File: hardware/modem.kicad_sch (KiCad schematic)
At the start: 30 parts, among them J11 Conn_01x02, Q3 PMOS, Q4 Q_NPN_BEC, U6 SN74AVC4T245PW, U7 SARA-R500S-61B

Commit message: HW: Update BOM
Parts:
- J11: value Conn_01x02 -> PRPC001DAAN-RC
- Q3: value PMOS -> FDN338P
- Q4: value Q_NPN_BEC -> MMBT3904-TP
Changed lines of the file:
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@@
 			)
 		)
-		(property "Value" "PMOS"
+		(property "Value" "FDN338P"
 			(at 30.48 84.836 90)
 			(effects
@@
 			)
 		)
-		(property "Value" "Conn_01x02"
+		(property "Value" "PRPC001DAAN-RC"
 			(at 49.53 163.83 0)
 			(effects
@@
 			)
 		)
-		(property "Value" "Q_NPN_BEC"
+		(property "Value" "MMBT3904-TP"
 			(at 64.77 165.0999 0)
 			(effects

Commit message: HW: Fix BOM
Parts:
- TP5: now left out of the parts list
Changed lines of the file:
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@@
 		(unit 1)
 		(exclude_from_sim no)
-		(in_bom yes)
+		(in_bom no)
 		(on_board yes)
 		(dnp no)

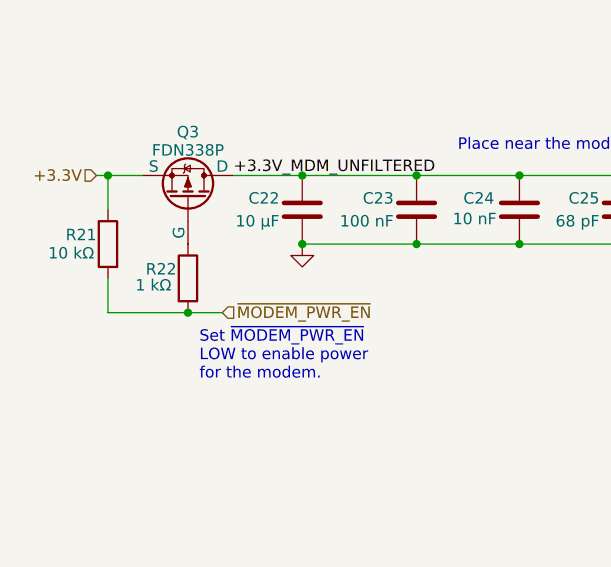
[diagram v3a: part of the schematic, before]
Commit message: HW: BOM consolidate
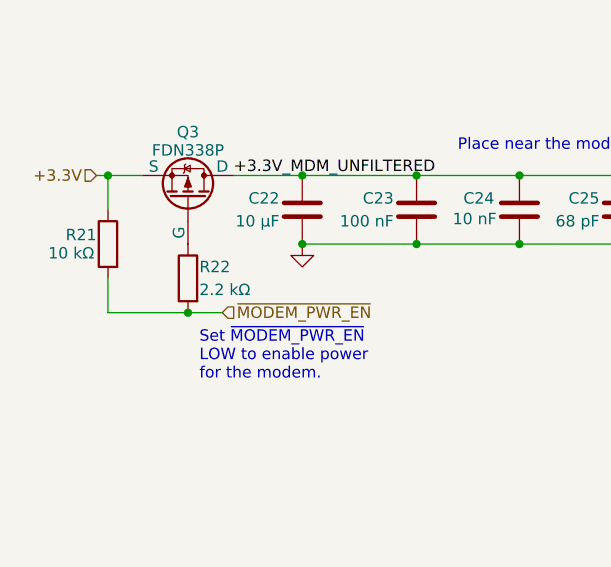
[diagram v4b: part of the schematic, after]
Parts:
- R22: value 1 kΩ -> 2.2 kΩ; Digi-Key Part Number 311-1.00KLRCT-ND -> 311-2.20KLRCT-ND; Manufacturer Part Number RC0402FR-071KL -> RC0402FR-072K2L
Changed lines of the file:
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@@
 	)
 	(junction
-		(at 30.48 102.87)
-		(diameter 0)
-		(color 0 0 0 0)
-	)
-	(junction
 		(at 170.18 101.6)
 		(diameter 0)
@@
 	)
 	(junction
+		(at 30.48 102.87)
+		(diameter 0)
+		(color 0 0 0 0)
+	)
+	(junction
 		(at 83.82 163.83)
 		(diameter 0)
@@
 	(wire
 		(pts
-			(xy 34.29 102.87) (xy 30.48 102.87)
+			(xy 55.88 87.63) (xy 67.31 87.63)
 		)
 		(stroke
@@
 	(wire
 		(pts
-			(xy 55.88 87.63) (xy 67.31 87.63)
+			(xy 154.94 83.82) (xy 157.48 83.82)
 		)
 		(stroke
@@
 	(wire
 		(pts
-			(xy 154.94 83.82) (xy 157.48 83.82)
+			(xy 270.51 109.22) (xy 274.32 109.22)
 		)
 		(stroke
@@
 	(wire
 		(pts
-			(xy 270.51 109.22) (xy 274.32 109.22)
+			(xy 66.04 156.21) (xy 67.31 156.21)
 		)
 		(stroke
@@
 	(wire
 		(pts
-			(xy 66.04 156.21) (xy 67.31 156.21)
+			(xy 30.48 102.87) (xy 34.29 102.87)
 		)
 		(stroke
@@
 	)
 	(symbol
-		(lib_id "Device:R")
-		(at 30.48 99.06 0)
+		(lib_id "power:GND")
+		(at 255.27 162.56 0)
+		(mirror y)
 		(unit 1)
 		(exclude_from_sim no)
@@
 		(on_board yes)
 		(dnp no)
-		(property "Reference" "R22"
-			(at 29.21 98.044 0)
-			(effects
-				(font
-					(size 1.27 1.27)
-				)
-				(justify right)
-			)
-		)
-		(property "Value" "1 kΩ"
-			(at 24.638 99.822 0)
-			(effects
-				(font
-					(size 1.27 1.27)
-				)
-				(justify left)
-			)
-		)
-		(property "Footprint" "perfect_footprints:0402_1005_perfect"
-			(at 28.702 99.06 90)
-			(effects
-				(font
-					(size 1.27 1.27)
-				)
-				(hide yes)
-			)
-		)
-		(property "Datasheet" "~"
-			(at 30.48 99.06 0)
+		(fields_autoplaced yes)
+		(property "Reference" "#PWR026"
+			(at 255.27 168.91 0)
 			(effects
 				(font
@@
 			)
 		)
-		(property "Description" ""
-			(at 30.48 99.06 0)
+		(property "Value" "GND"
+			(at 255.27 167.64 0)
 			(effects
 				(font
@@
 			)
 		)
-		(property "Manufacturer" "YAGEO"
-			(at 30.48 99.06 0)
+		(property "Footprint" ""
+			(at 255.27 162.56 0)
 			(effects
 				(font
@@
 			)
 		)
-		(property "Manufacturer Part Number" "RC0402FR-071KL"
-			(at 30.48 99.06 0)
+		(property "Datasheet" ""
+			(at 255.27 162.56 0)
 			(effects
 				(font
@@
 			)
 		)
-		(property "Digi-Key Part Number" "311-1.00KLRCT-ND"
-			(at 30.48 99.06 0)
+		(property "Description" "Power symbol creates a global label with name \"GND\" , ground"
+			(at 255.27 162.56 0)
 			(effects
 				(font
@@
 		(pin "1"
 		)
-		(pin "2"
-		)
 		(instances
 			(project "iida_devkit"
 				(path "/b12a6e25-97fb-4aba-bc96-af8db389bb9a/3723475b-e956-4027-ac40-e47346743900"
-					(reference "R22")
+					(reference "#PWR026")
 					(unit 1)
 				)
@@
 	)
 	(symbol
-		(lib_id "power:GND")
-		(at 255.27 162.56 0)
+		(lib_id "Device:R")
+		(at 30.48 99.06 0)
 		(mirror y)
 		(unit 1)
@@
 		(on_board yes)
 		(dnp no)
-		(fields_autoplaced yes)
-		(property "Reference" "#PWR026"
-			(at 255.27 168.91 0)
+		(property "Reference" "R22"
+			(at 31.75 97.79 0)
+			(effects
+				(font
+					(size 1.27 1.27)
+				)
+				(justify right)
+			)
+		)
+		(property "Value" "2.2 kΩ"
+			(at 31.75 100.33 0)
+			(effects
+				(font
+					(size 1.27 1.27)
+				)
+				(justify right)
+			)
+		)
+		(property "Footprint" "perfect_footprints:0402_1005_perfect"
+			(at 32.258 99.06 90)
 			(effects
 				(font
@@
 			)
 		)
-		(property "Value" "GND"
-			(at 255.27 167.64 0)
+		(property "Datasheet" "~"
+			(at 30.48 99.06 0)
 			(effects
 				(font
@@
 			)
 		)
-		(property "Footprint" ""
-			(at 255.27 162.56 0)
+		(property "Description" ""
+			(at 30.48 99.06 0)
 			(effects
 				(font
@@
 			)
 		)
-		(property "Datasheet" ""
-			(at 255.27 162.56 0)
+		(property "Digi-Key Part Number" "311-2.20KLRCT-ND"
+			(at 30.48 99.06 0)
 			(effects
 				(font
@@
 			)
 		)
-		(property "Description" "Power symbol creates a global label with name \"GND\" , ground"
-			(at 255.27 162.56 0)
+		(property "Manufacturer" "YAGEO"
+			(at 30.48 99.06 0)
+			(effects
+				(font
+					(size 1.27 1.27)
+				)
+				(hide yes)
+			)
+		)
+		(property "Manufacturer Part Number" "RC0402FR-072K2L"
+			(at 30.48 99.06 0)
 			(effects
 				(font
@@
 			)
 		)
+		(pin "2"
+		)
 		(pin "1"
 		)
@@
 			(project "iida_devkit"
 				(path "/b12a6e25-97fb-4aba-bc96-af8db389bb9a/3723475b-e956-4027-ac40-e47346743900"
-					(reference "#PWR026")
+					(reference "R22")
 					(unit 1)
 				)

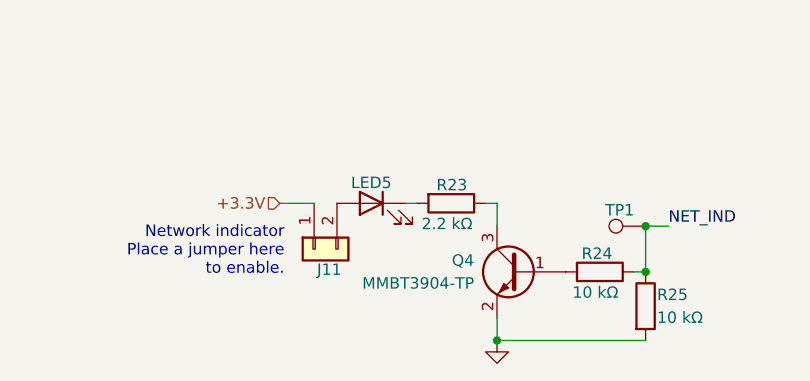
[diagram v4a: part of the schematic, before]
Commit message: HW: Replace chinese NPN BJT
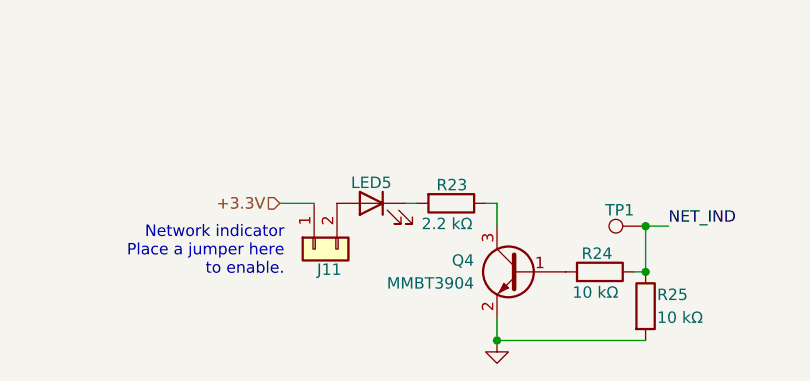
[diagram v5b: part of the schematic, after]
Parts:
- Q4: value MMBT3904-TP -> MMBT3904; Digi-Key Part Number MMBT3904TPMSCT-ND -> 4878-MMBT3904CT-ND; Manufacturer Micro Commercial Co -> Diotec Semiconductor; Manufacturer Part Number MMBT3904-TP -> MMBT3904
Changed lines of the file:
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@@
 			)
 		)
-		(property "Value" "MMBT3904-TP"
+		(property "Value" "MMBT3904"
 			(at 64.77 165.0999 0)
 			(effects
@@
 			)
 		)
-		(property "Digi-Key Part Number" "MMBT3904TPMSCT-ND"
+		(property "Digi-Key Part Number" "4878-MMBT3904CT-ND"
 			(at 69.85 163.83 0)
 			(effects
@@
 			)
 		)
-		(property "Manufacturer" "Micro Commercial Co"
+		(property "Manufacturer" "Diotec Semiconductor"
 			(at 69.85 163.83 0)
 			(effects
@@
 			)
 		)
-		(property "Manufacturer Part Number" "MMBT3904-TP"
+		(property "Manufacturer Part Number" "MMBT3904"
 			(at 69.85 163.83 0)
 			(effects

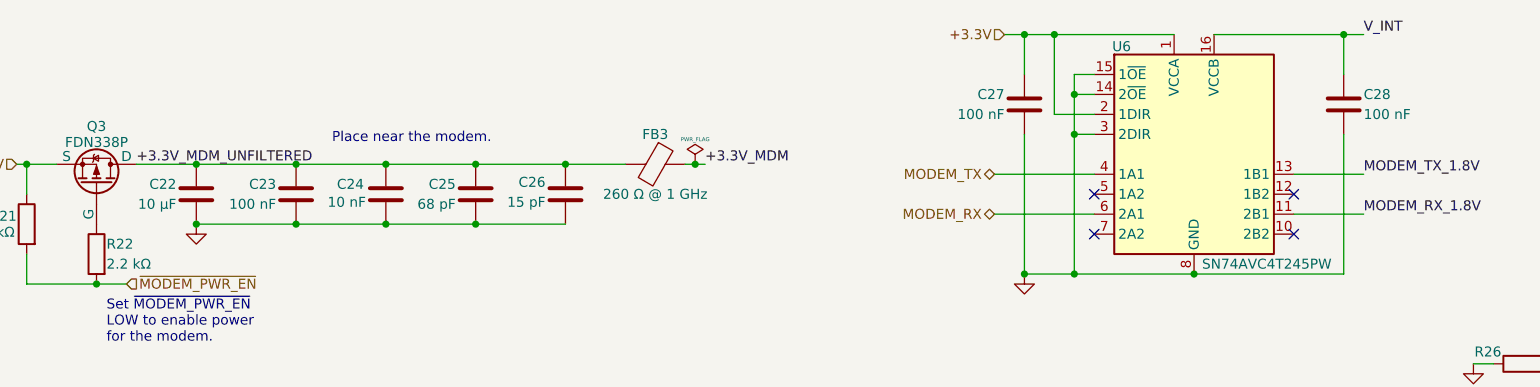
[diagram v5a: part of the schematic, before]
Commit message: HW: Connect +BATT to MCU
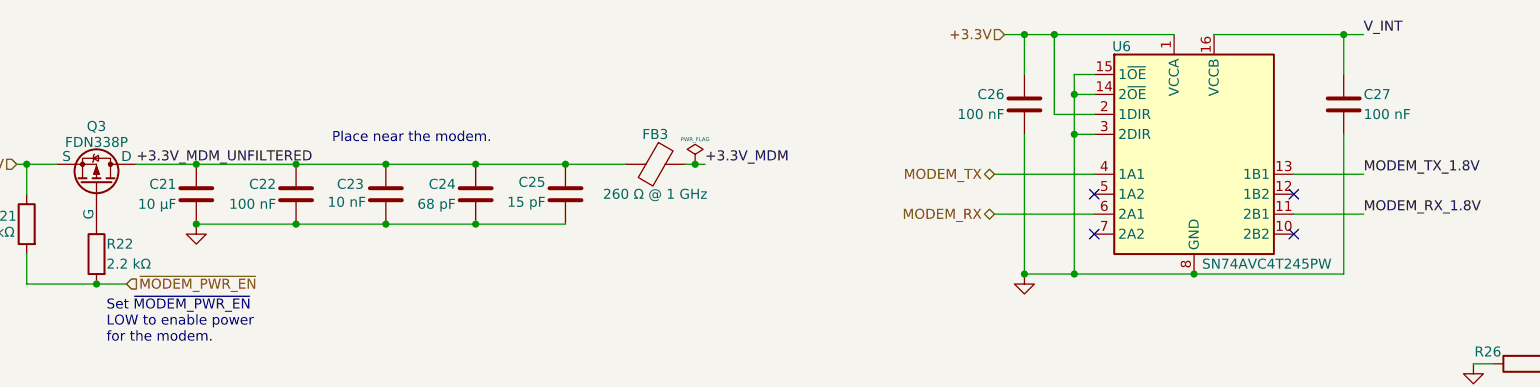
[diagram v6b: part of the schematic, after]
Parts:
- renumbered C22 to C21, C23 to C22, C24 to C23, C25 to C24, C26 to C25, C27 to C26, C28 to C27
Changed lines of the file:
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@@
 	(title_block
 		(title "Iida devkit")
-		(date "2024-09-22")
-		(rev "v4.1.0")
+		(date "2024-09-25")
+		(rev "v4.2.0")
 	)
 	(junction
@@
 		(on_board yes)
 		(dnp no)
-		(property "Reference" "C24"
+		(property "Reference" "C23"
 			(at 64.516 90.17 0)
 			(effects
@@
 			(project "iida_devkit"
 				(path "/b12a6e25-97fb-4aba-bc96-af8db389bb9a/3723475b-e956-4027-ac40-e47346743900"
-					(reference "C24")
+					(reference "C23")
 					(unit 1)
 				)
@@
 		(on_board yes)
 		(dnp no)
-		(property "Reference" "C22"
+		(property "Reference" "C21"
 			(at 40.64 90.17 0)
 			(effects
@@
 			(project "iida_devkit"
 				(path "/b12a6e25-97fb-4aba-bc96-af8db389bb9a/3723475b-e956-4027-ac40-e47346743900"
-					(reference "C22")
+					(reference "C21")
 					(unit 1)
 				)
@@
 		(on_board yes)
 		(dnp no)
-		(property "Reference" "C25"
+		(property "Reference" "C24"
 			(at 76.2 90.17 0)
 			(effects
@@
 			(project "iida_devkit"
 				(path "/b12a6e25-97fb-4aba-bc96-af8db389bb9a/3723475b-e956-4027-ac40-e47346743900"
-					(reference "C25")
+					(reference "C24")
 					(unit 1)
 				)
@@
 		(on_board yes)
 		(dnp no)
-		(property "Reference" "#FLG05"
+		(property "Reference" "#FLG06"
 			(at 106.68 85.725 0)
 			(effects
@@
 			(project "iida_devkit"
 				(path "/b12a6e25-97fb-4aba-bc96-af8db389bb9a/3723475b-e956-4027-ac40-e47346743900"
-					(reference "#FLG05")
+					(reference "#FLG06")
 					(unit 1)
 				)
@@
 		(on_board yes)
 		(dnp no)
-		(property "Reference" "C28"
+		(property "Reference" "C27"
 			(at 191.77 78.74 0)
 			(effects
@@
 			(project "iida_devkit"
 				(path "/b12a6e25-97fb-4aba-bc96-af8db389bb9a/3723475b-e956-4027-ac40-e47346743900"
-					(reference "C28")
+					(reference "C27")
 					(unit 1)
 				)
@@
 		(on_board yes)
 		(dnp no)
-		(property "Reference" "C27"
+		(property "Reference" "C26"
 			(at 146.05 78.74 0)
 			(effects
@@
 			(project "iida_devkit"
 				(path "/b12a6e25-97fb-4aba-bc96-af8db389bb9a/3723475b-e956-4027-ac40-e47346743900"
-					(reference "C27")
+					(reference "C26")
 					(unit 1)
 				)
@@
 		(on_board yes)
 		(dnp no)
-		(property "Reference" "C26"
+		(property "Reference" "C25"
 			(at 87.63 89.916 0)
 			(effects
@@
 			(project "iida_devkit"
 				(path "/b12a6e25-97fb-4aba-bc96-af8db389bb9a/3723475b-e956-4027-ac40-e47346743900"
-					(reference "C26")
+					(reference "C25")
 					(unit 1)
 				)
@@
 		(on_board yes)
 		(dnp no)
-		(property "Reference" "C23"
+		(property "Reference" "C22"
 			(at 53.34 90.17 0)
 			(effects
@@
 			(project "iida_devkit"
 				(path "/b12a6e25-97fb-4aba-bc96-af8db389bb9a/3723475b-e956-4027-ac40-e47346743900"
-					(reference "C23")
+					(reference "C22")
 					(unit 1)
 				)

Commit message: HW: Update components
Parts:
- C22, C26, C27: Digi-Key Part Number 490-7998-1-ND -> 732-7513-1-ND; Manufacturer Murata Electronics -> Würth Elektronik; Manufacturer Part Number GCM155R71C104KA55J -> 885012205018
- C24: Digi-Key Part Number 490-12653-1-ND -> 732-7474-1-ND; Manufacturer Murata Electronics -> Würth Elektronik; Manufacturer Part Number GCM1555C1H680JA16D -> 885012005060
- C25: Digi-Key Part Number 490-5888-1-ND -> 732-7470-1-ND; Manufacturer Murata Electronics -> Würth Elektronik; Manufacturer Part Number GRM1555C1H150JA01D -> 885012005056
- LED5: value LS T67K-K1L2-1-0-2-R18-Z -> 150141YS73100; Digi-Key Part Number 475-LST67K-K1L2-1-ZCT-ND -> 732-5004-1-ND; Manufacturer ams-OSRAM USA INC. -> Würth Elektronik; Manufacturer Part Number LS T67K-K1L2-1-0-2-R18-Z -> 150141YS73100
- Q3: value FDN338P -> IRLML2246TRPBF; Digi-Key Part Number FDN338PCT-ND -> IRLML2246TRPBFCT-ND; Manufacturer onsemi -> Infineon Technologies; Manufacturer Part Number FDN338P -> IRLML2246TRPBF
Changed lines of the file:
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@@
 			)
 		)
-		(property "Value" "LS T67K-K1L2-1-0-2-R18-Z"
+		(property "Value" "150141YS73100"
 			(at 53.34 160.02 0)
 			(effects
@@
 			)
 		)
-		(property "Manufacturer" "ams-OSRAM USA INC."
+		(property "Manufacturer" "Würth Elektronik"
 			(at 53.34 156.21 90)
 			(effects
@@
 			)
 		)
-		(property "Manufacturer Part Number" "LS T67K-K1L2-1-0-2-R18-Z"
+		(property "Manufacturer Part Number" "150141YS73100"
 			(at 53.34 156.21 90)
 			(effects
@@
 			)
 		)
-		(property "Digi-Key Part Number" "475-LST67K-K1L2-1-ZCT-ND"
+		(property "Digi-Key Part Number" "732-5004-1-ND"
 			(at 53.34 156.21 90)
 			(effects
@@
 			)
 		)
-		(property "Value" "FDN338P"
+		(property "Value" "IRLML2246TRPBF"
 			(at 30.48 84.836 90)
 			(effects
@@
 			)
 		)
-		(property "Digi-Key Part Number" "FDN338PCT-ND"
+		(property "Digi-Key Part Number" "IRLML2246TRPBFCT-ND"
 			(at 30.48 90.17 0)
 			(effects
@@
 			)
 		)
-		(property "Manufacturer" "onsemi"
+		(property "Manufacturer" "Infineon Technologies"
 			(at 30.48 90.17 0)
 			(effects
@@
 			)
 		)
-		(property "Manufacturer Part Number" "FDN338P"
+		(property "Manufacturer Part Number" "IRLML2246TRPBF"
 			(at 30.48 90.17 0)
 			(effects
@@
 			)
 		)
-		(property "Digi-Key Part Number" "490-12653-1-ND"
+		(property "Digi-Key Part Number" "732-7474-1-ND"
 			(at 78.74 91.44 0)
 			(effects
@@
 			)
 		)
-		(property "Manufacturer" "Murata Electronics"
+		(property "Manufacturer" "Würth Elektronik"
 			(at 78.74 91.44 0)
 			(effects
@@
 			)
 		)
-		(property "Manufacturer Part Number" "GCM1555C1H680JA16D"
+		(property "Manufacturer Part Number" "885012005060"
 			(at 78.74 91.44 0)
 			(effects
@@
 			)
 		)
-		(property "Manufacturer" "Murata Electronics"
+		(property "Manufacturer" "Würth Elektronik"
 			(at 189.23 80.01 0)
 			(effects
@@
 			)
 		)
-		(property "Manufacturer Part Number" "GCM155R71C104KA55J"
+		(property "Manufacturer Part Number" "885012205018"
 			(at 189.23 80.01 0)
 			(effects
@@
 			)
 		)
-		(property "Digi-Key Part Number" "490-7998-1-ND"
+		(property "Digi-Key Part Number" "732-7513-1-ND"
 			(at 189.23 80.01 0)
 			(effects
@@
 			)
 		)
-		(property "Manufacturer" "Murata Electronics"
+		(property "Manufacturer" "Würth Elektronik"
 			(at 148.59 80.01 0)
 			(effects
@@
 			)
 		)
-		(property "Manufacturer Part Number" "GCM155R71C104KA55J"
+		(property "Manufacturer Part Number" "885012205018"
 			(at 148.59 80.01 0)
 			(effects
@@
 			)
 		)
-		(property "Digi-Key Part Number" "490-7998-1-ND"
+		(property "Digi-Key Part Number" "732-7513-1-ND"
 			(at 148.59 80.01 0)
 			(effects
@@
 			)
 		)
-		(property "Digi-Key Part Number" "490-5888-1-ND"
+		(property "Digi-Key Part Number" "732-7470-1-ND"
 			(at 90.17 91.44 0)
 			(effects
@@
 			)
 		)
-		(property "Manufacturer" "Murata Electronics"
+		(property "Manufacturer" "Würth Elektronik"
 			(at 90.17 91.44 0)
 			(effects
@@
 			)
 		)
-		(property "Manufacturer Part Number" "GRM1555C1H150JA01D"
+		(property "Manufacturer Part Number" "885012005056"
 			(at 90.17 91.44 0)
 			(effects
@@
 			)
 		)
-		(property "Manufacturer" "Murata Electronics"
+		(property "Manufacturer" "Würth Elektronik"
 			(at 55.88 91.44 0)
 			(effects
@@
 			)
 		)
-		(property "Manufacturer Part Number" "GCM155R71C104KA55J"
+		(property "Manufacturer Part Number" "885012205018"
 			(at 55.88 91.44 0)
 			(effects
@@
 			)
 		)
-		(property "Digi-Key Part Number" "490-7998-1-ND"
+		(property "Digi-Key Part Number" "732-7513-1-ND"
 			(at 55.88 91.44 0)
 			(effects
